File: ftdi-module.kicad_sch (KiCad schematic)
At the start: 50 parts, among them J1 USB3106-30-0230-A, U2 ISO1641, U3 NCP163ASN330T1G, U5 FT4232H-56Q, Y1 KX-7_12,MHz

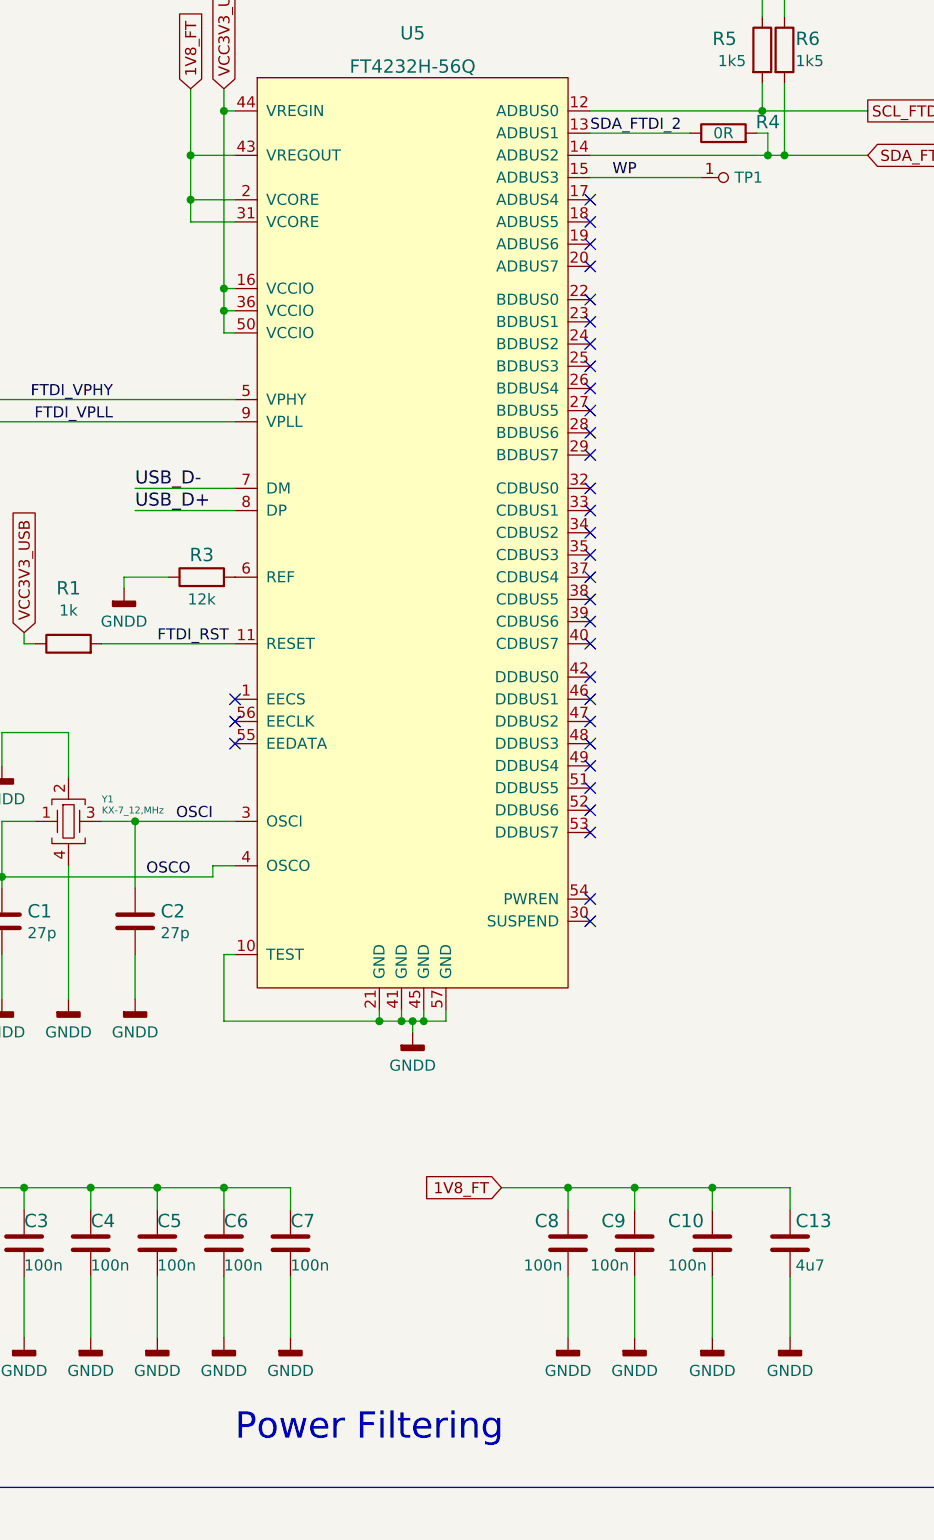
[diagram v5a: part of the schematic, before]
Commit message: Finished replacing FTDI chip on the PCB
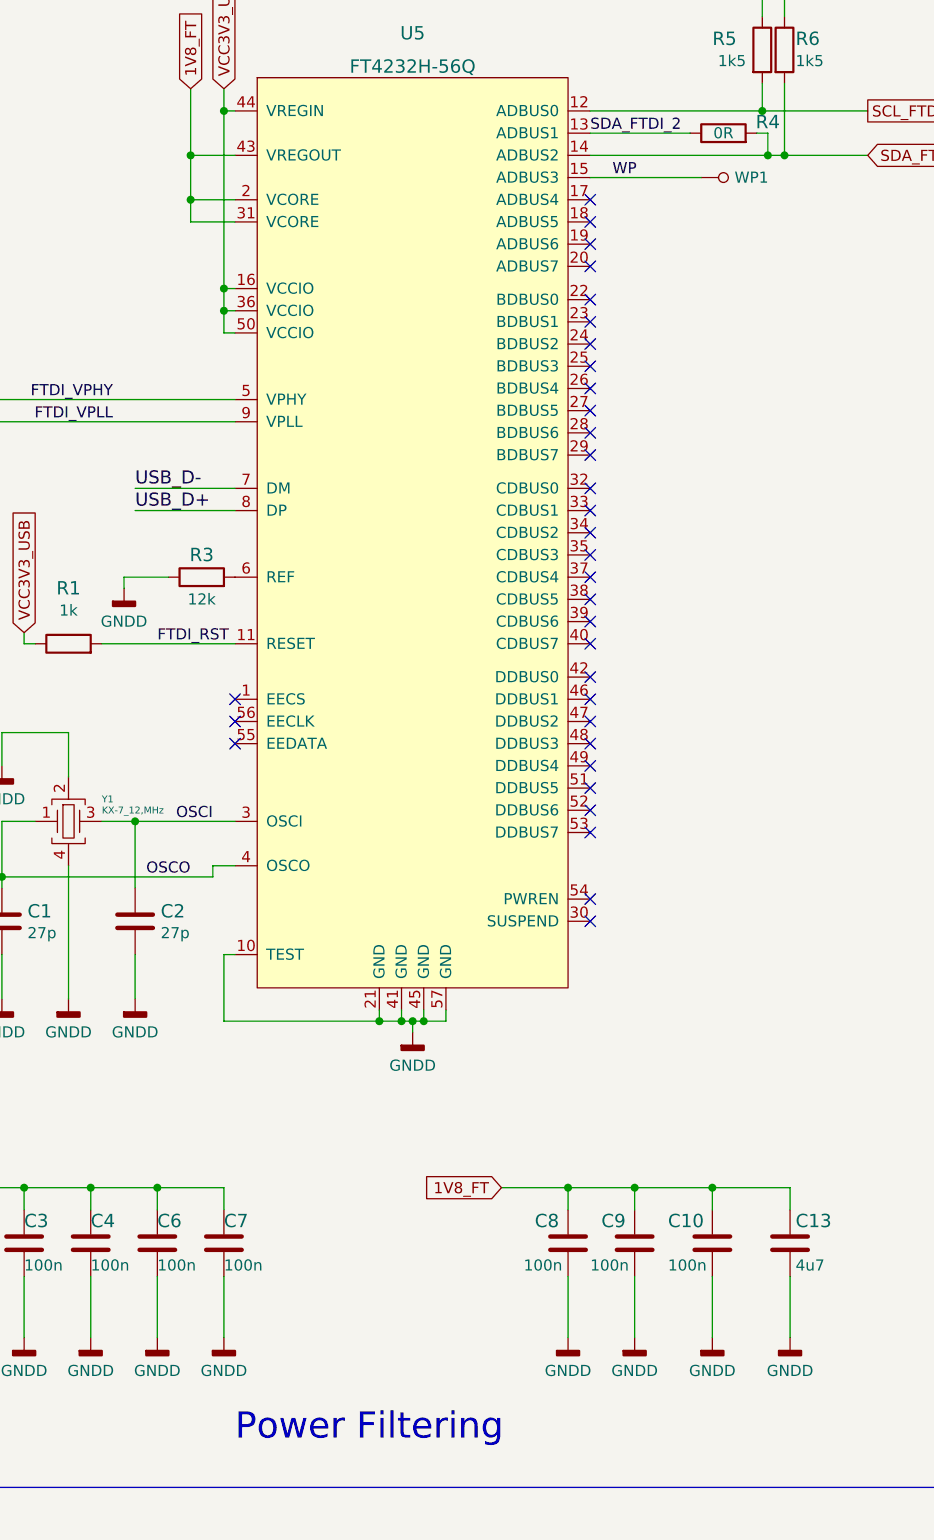
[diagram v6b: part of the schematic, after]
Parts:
- removed C5: C_100n_0402, nuc-compute-cluster-power-breakout-footprints:0402-cap, symbol nuc-compute-cluster-power-breakout:C_100n_0402
- removed TP1: TP, antmicro-footprints:TP-R-1.5, symbol antmicroTestPoints:TP
- added WP1: TP_SMD1MM, antmicro-footprints:Testpoint_smd_1mm, symbol antmicroTestPoints:TP_SMD1MM
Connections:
- net WP: now also WP1.1
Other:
- moved on the sheet: C6, C7
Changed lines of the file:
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@@
   (junction (at 167.005 26.67) (diameter 0) (color 0 0 0 0)
   )
-  (junction (at 105.41 165.1) (diameter 0) (color 0 0 0 0)
-  )
   (junction (at 36.83 74.93) (diameter 0) (color 0 0 0 0)
   )
   (junction (at 125.73 146.05) (diameter 0) (color 0 0 0 0)
   )
-  (junction (at 97.79 165.1) (diameter 0) (color 0 0 0 0)
-  )
   (junction (at 91.44 217.805) (diameter 0) (color 0 0 0 0)
   )
   (junction (at 152.4 165.1) (diameter 0) (color 0 0 0 0)
   )
+  (junction (at 97.79 165.1) (diameter 0) (color 0 0 0 0)
+  )
   (junction (at 105.41 64.77) (diameter 0) (color 0 0 0 0)
   )
@@
   (junction (at 302.895 130.81) (diameter 0) (color 0 0 0 0)
   )
-  (no_connect (at 147.32 66.04))
-  (no_connect (at 147.32 68.58))
-  (no_connect (at 147.32 71.12))
-  (no_connect (at 147.32 52.07))
-  (no_connect (at 147.32 54.61))
-  (no_connect (at 147.32 57.15))
-  (no_connect (at 147.32 59.69))
-  (no_connect (at 147.32 63.5))
   (no_connect (at 147.32 73.66))
   (no_connect (at 147.32 76.2))
@@
   (no_connect (at 147.32 121.92))
   (no_connect (at 147.32 124.46))
+  (no_connect (at 147.32 66.04))
+  (no_connect (at 147.32 68.58))
+  (no_connect (at 147.32 71.12))
+  (no_connect (at 147.32 52.07))
+  (no_connect (at 147.32 54.61))
+  (no_connect (at 147.32 57.15))
+  (no_connect (at 147.32 59.69))
+  (no_connect (at 147.32 63.5))
   (no_connect (at 106.68 114.3))
   (no_connect (at 106.68 111.76))
@@
     (stroke (width 0) (type default) (color 0 0 0 0))
   )
+  (wire (pts (xy 97.79 165.1) (xy 105.41 165.1))
+    (stroke (width 0) (type default) (color 0 0 0 0))
+  )
   (wire (pts (xy 161.29 175.26) (xy 161.29 182.245))
     (stroke (width 0) (type default) (color 0 0 0 0))
@@
     (stroke (width 0) (type default) (color 0 0 0 0))
   )
-  (wire (pts (xy 97.79 165.1) (xy 105.41 165.1))
-    (stroke (width 0) (type default) (color 0 0 0 0))
-  )
   (wire (pts (xy 46.99 74.93) (xy 36.83 74.93))
     (stroke (width 0) (type default) (color 0 0 0 0))
@@
     (stroke (width 0) (type default) (color 0 0 0 0))
   )
-  (wire (pts (xy 105.41 175.26) (xy 105.41 182.245))
+  (wire (pts (xy 97.79 175.26) (xy 97.79 182.245))
     (stroke (width 0) (type default) (color 0 0 0 0))
   )
@@
     (stroke (width 0) (type default) (color 0 0 0 0))
   )
-  (wire (pts (xy 97.79 175.26) (xy 97.79 182.245))
-    (stroke (width 0) (type default) (color 0 0 0 0))
-  )
   (wire (pts (xy 101.6 46.99) (xy 106.68 46.99))
     (stroke (width 0) (type default) (color 0 0 0 0))
@@
     (stroke (width 0) (type default) (color 0 0 0 0))
   )
-  (wire (pts (xy 105.41 165.1) (xy 113.03 165.1))
-    (stroke (width 0) (type default) (color 0 0 0 0))
-  )
   (wire (pts (xy 321.31 86.36) (xy 328.93 86.36))
     (stroke (width 0) (type default) (color 0 0 0 0))
@@
     (stroke (width 0) (type default) (color 0 0 0 0))
   )
-  (wire (pts (xy 113.03 165.1) (xy 113.03 167.64))
+  (wire (pts (xy 105.41 165.1) (xy 105.41 167.64))
     (stroke (width 0) (type default) (color 0 0 0 0))
   )
@@
     (stroke (width 0) (type default) (color 0 0 0 0))
   )
-  (wire (pts (xy 105.41 167.64) (xy 105.41 165.1))
+  (wire (pts (xy 97.79 167.64) (xy 97.79 165.1))
     (stroke (width 0) (type default) (color 0 0 0 0))
   )
@@
     (stroke (width 0) (type default) (color 0 0 0 0))
   )
-  (wire (pts (xy 113.03 175.26) (xy 113.03 182.245))
+  (wire (pts (xy 105.41 175.26) (xy 105.41 182.245))
     (stroke (width 0) (type default) (color 0 0 0 0))
   )
@@
     (stroke (width 0) (type default) (color 0 0 0 0))
   )
-  (wire (pts (xy 97.79 167.64) (xy 97.79 165.1))
-    (stroke (width 0) (type default) (color 0 0 0 0))
-  )
   (wire (pts (xy 100.965 233.045) (xy 104.14 233.045))
     (stroke (width 0) (type default) (color 0 0 0 0))
@@
   (symbol (lib_id "nuc-compute-cluster-power-breakout:C_100n_0402") (at 97.79 171.45 0) (unit 1)
     (in_bom yes) (on_board yes)
-    (property "Reference" "C5" (id 0) (at 97.79 168.91 0)
+    (property "Reference" "C6" (id 0) (at 97.79 168.91 0)
       (effects (font (size 1.524 1.524)) (justify left))
     )
@@
   (symbol (lib_id "nuc-compute-cluster-power-breakout:C_100n_0402") (at 105.41 171.45 0) (unit 1)
     (in_bom yes) (on_board yes)
-    (property "Reference" "C6" (id 0) (at 105.41 168.91 0)
+    (property "Reference" "C7" (id 0) (at 105.41 168.91 0)
       (effects (font (size 1.524 1.524)) (justify left))
     )
@@
     (pin "2")
   )
-  (symbol (lib_id "nuc-compute-cluster-power-breakout:C_100n_0402") (at 113.03 171.45 0) (unit 1)
-    (in_bom yes) (on_board yes)
-    (property "Reference" "C7" (id 0) (at 113.03 168.91 0)
-      (effects (font (size 1.524 1.524)) (justify left))
-    )
-    (property "Value" "C_100n_0402" (id 1) (at 113.03 175.26 0)
-      (effects (font (size 1.524 1.524)) hide)
-    )
-    (property "Footprint" "nuc-compute-cluster-power-breakout-footprints:0402-cap" (id 2) (at 118.11 166.37 0)
-      (effects (font (size 1.524 1.524)) (justify left) hide)
-    )
-    (property "Datasheet" "" (id 3) (at 113.03 171.45 0)
-      (effects (font (size 1.27 1.27)) hide)
-    )
-    (property "Manufacturer" "Murata" (id 4) (at 118.11 161.29 0)
-      (effects (font (size 1.524 1.524)) (justify left) hide)
-    )
-    (property "MPN" "GRM155R61H104KE14D" (id 5) (at 118.11 163.83 0)
-      (effects (font (size 1.524 1.524)) (justify left) hide)
-    )
-    (property "Val" "100n" (id 6) (at 113.03 173.99 0)
-      (effects (font (size 1.27 1.27)) (justify left))
-    )
-    (pin "1")
-    (pin "2")
-  )
   (symbol (lib_id "nuc-compute-cluster-power-breakout:C_100n_0402") (at 152.4 171.45 0) (unit 1)
     (in_bom yes) (on_board yes)
@@
     (pin "1")
   )
-  (symbol (lib_id "nuc-compute-cluster-power-breakout:GNDD") (at 113.03 182.245 0) (unit 1)
-    (in_bom yes) (on_board yes)
-    (property "Reference" "#PWR014" (id 0) (at 113.03 188.595 0)
-      (effects (font (size 1.27 1.27)) hide)
-    )
-    (property "Value" "GNDD" (id 1) (at 113.03 186.055 0))
-    (property "Footprint" "nuc-compute-cluster-power-breakout-footprints:" (id 2) (at 113.03 182.245 0)
-      (effects (font (size 1.27 1.27)) hide)
-    )
-    (property "Datasheet" "" (id 3) (at 113.03 182.245 0)
-      (effects (font (size 1.27 1.27)) hide)
-    )
-    (pin "1")
-  )
   (symbol (lib_id "nuc-compute-cluster-power-breakout:GNDD") (at 105.41 182.245 0) (unit 1)
     (in_bom yes) (on_board yes)
-    (property "Reference" "#PWR013" (id 0) (at 105.41 188.595 0)
+    (property "Reference" "#PWR014" (id 0) (at 105.41 188.595 0)
       (effects (font (size 1.27 1.27)) hide)
     )
@@
   (symbol (lib_id "nuc-compute-cluster-power-breakout:GNDD") (at 97.79 182.245 0) (unit 1)
     (in_bom yes) (on_board yes)
-    (property "Reference" "#PWR011" (id 0) (at 97.79 188.595 0)
+    (property "Reference" "#PWR013" (id 0) (at 97.79 188.595 0)
       (effects (font (size 1.27 1.27)) hide)
     )
@@
     (pin "1")
   )
+  (symbol (lib_id "antmicroTestPoints:TP_SMD1MM") (at 162.56 49.53 90) (unit 1)
+    (in_bom yes) (on_board yes) (fields_autoplaced)
+    (property "Reference" "WP1" (id 0) (at 163.83 49.5299 90)
+      (effects (font (size 1.27 1.27)) (justify right))
+    )
+    (property "Value" "TP_SMD1MM" (id 1) (at 165.1 49.53 0)
+      (effects (font (size 1.27 1.27)) hide)
+    )
+    (property "Footprint" "antmicro-footprints:Testpoint_smd_1mm" (id 2) (at 157.48 44.45 0)
+      (effects (font (size 1.524 1.524)) (justify left) hide)
+    )
+    (property "Datasheet" "" (id 3) (at 154.94 44.45 0)
+      (effects (font (size 1.524 1.524)) (justify left) hide)
+    )
+    (pin "1")
+  )
   (symbol (lib_id "nuc-compute-cluster-power-breakout:R_12k_0402") (at 102.87 95.25 0) (unit 1)
     (in_bom yes) (on_board yes)
@@
     (pin "2")
   )
-  (symbol (lib_id "antmicroTestPoints:TP") (at 162.56 49.53 90) (unit 1)
-    (in_bom yes) (on_board yes) (fields_autoplaced)
-    (property "Reference" "TP1" (id 0) (at 163.83 49.5299 90)
-      (effects (font (size 1.27 1.27)) (justify right))
-    )
-    (property "Value" "TP" (id 1) (at 162.56 49.53 0)
-      (effects (font (size 1.27 1.27)) hide)
-    )
-    (property "Footprint" "antmicro-footprints:TP-R-1.5" (id 2) (at 162.56 49.53 0)
-      (effects (font (size 1.27 1.27)) hide)
-    )
-    (property "Datasheet" "" (id 3) (at 162.56 49.53 0)
-      (effects (font (size 1.27 1.27)) hide)
-    )
-    (pin "1")
-  )
   (symbol (lib_id "nuc-compute-cluster-power-breakout:GNDD") (at 64.77 90.17 0) (mirror y) (unit 1)

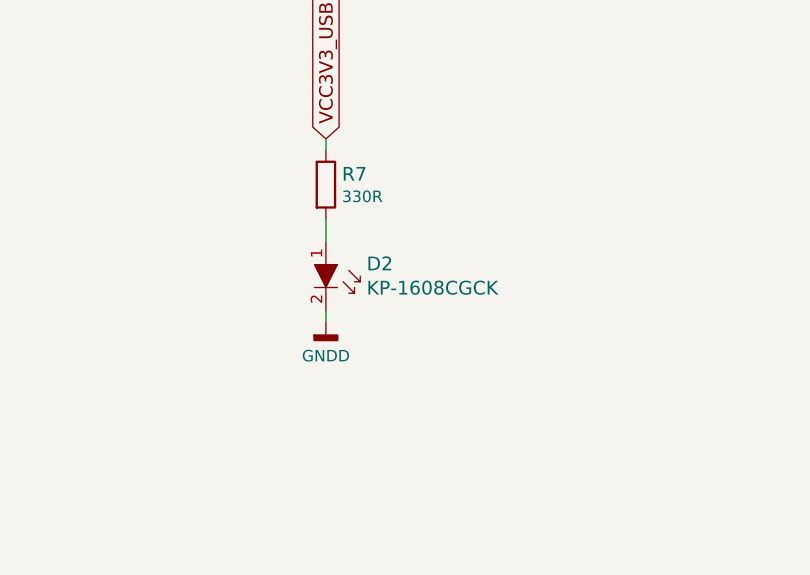
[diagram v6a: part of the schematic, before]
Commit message: Added LED indicators
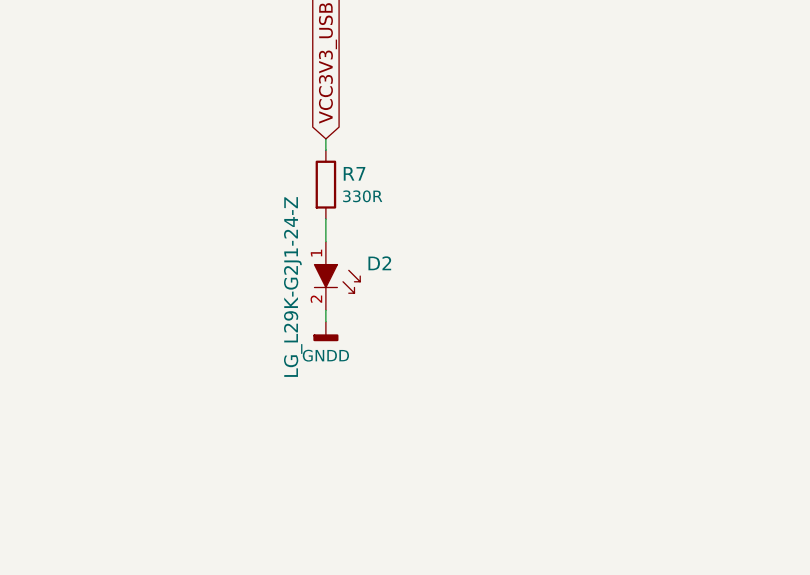
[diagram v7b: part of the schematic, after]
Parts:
- D2: value KP-1608CGCK -> LG_L29K-G2J1-24-Z; symbol nuc-compute-cluster-power-breakout:KP-1608CGCK -> nuc-compute-cluster-power-breakout:LG_L29K-G2J1-24-Z; MPN KP-1608CGCK -> LG L29K-G2J1-24-Z; Manufacturer KINGBRIGHT -> OSRAM Opto Semiconductors Inc.
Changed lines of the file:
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@@
     (pin "2")
   )
-  (symbol (lib_id "nuc-compute-cluster-power-breakout:KP-1608CGCK") (at 269.875 227.965 270) (unit 1)
+  (symbol (lib_id "nuc-compute-cluster-power-breakout:LG_L29K-G2J1-24-Z") (at 269.875 227.965 270) (unit 1)
     (in_bom yes) (on_board yes)
     (property "Reference" "D2" (id 0) (at 274.3962 225.3488 90)
       (effects (font (size 1.524 1.524)) (justify left))
     )
-    (property "Value" "KP-1608CGCK" (id 1) (at 274.3962 228.0412 90)
-      (effects (font (size 1.524 1.524)) (justify left))
+    (property "Value" "LG_L29K-G2J1-24-Z" (id 1) (at 266.065 227.965 0)
+      (effects (font (size 1.524 1.524)))
     )
     (property "Footprint" "nuc-compute-cluster-power-breakout-footprints:LED_0603" (id 2) (at 274.955 233.045 0)
       (effects (font (size 1.524 1.524)) (justify left) hide)
     )
-    (property "Datasheet" "http://www.farnell.com/datasheets/2045956.pdf" (id 3) (at 277.495 233.045 0)
+    (property "Datasheet" "https://dammedia.osram.info/media/resource/hires/osram-dam-2493945/LG%20L29K.pdf" (id 3) (at 277.495 233.045 0)
       (effects (font (size 1.524 1.524)) (justify left) hide)
     )
-    (property "MPN" "KP-1608CGCK" (id 4) (at 282.575 233.045 0)
+    (property "MPN" "LG L29K-G2J1-24-Z" (id 4) (at 282.575 233.045 0)
       (effects (font (size 1.524 1.524)) (justify left) hide)
     )
-    (property "Manufacturer" "KINGBRIGHT" (id 5) (at 285.623 233.299 0)
+    (property "Manufacturer" "OSRAM Opto Semiconductors Inc." (id 5) (at 297.815 233.045 0)
       (effects (font (size 1.524 1.524)) (justify left) hide)
     )
